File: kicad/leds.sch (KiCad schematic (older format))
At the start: 85 parts, among them U6 74HC154

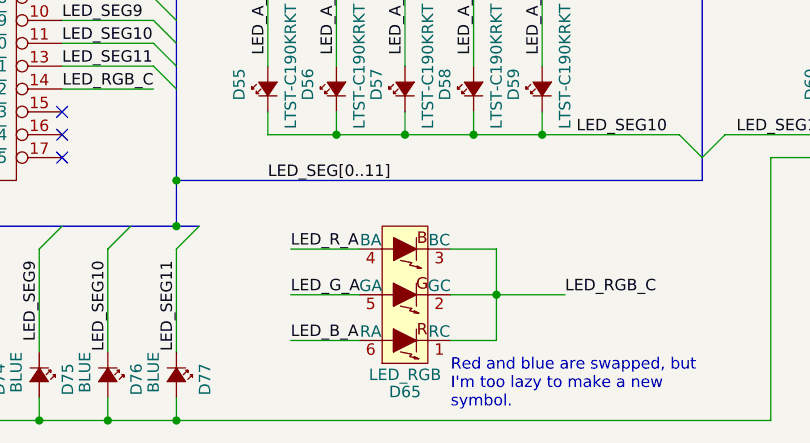
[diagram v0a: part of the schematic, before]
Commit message: Added footprints for most major components
We are missing almost all passives
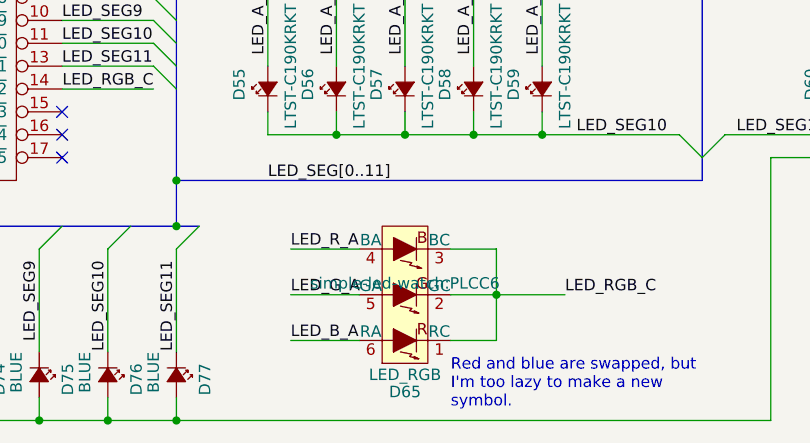
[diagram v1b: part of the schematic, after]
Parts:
- D65: footprint (none) -> simple-led-watch:PLCC6
- U6: footprint (none) -> simple-led-watch:DHVQFN24
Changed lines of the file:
@@
 F 0 "U6" H 3200 4750 50  0000 C CNN
 F 1 "74HC154" H 3200 6550 50  0000 C CNN
-F 2 "" H 3200 5500 50  0001 C CNN
+F 2 "simple-led-watch:DHVQFN24" H 3200 5500 50  0001 C CNN
 F 3 "" H 3200 5500 50  0001 C CNN
 F 4 "568-8858-1-ND" H 3200 5700 60  0001 C CNN "Part No."
@@
 LED_C_MUX3
 $Comp
-L +3.3V #PWR41
+L +3.3V #PWR041
 U 1 1 5802731F
 P 2600 4900
-F 0 "#PWR41" H 2600 4750 50  0001 C CNN
+F 0 "#PWR041" H 2600 4750 50  0001 C CNN
 F 1 "+3.3V" H 2600 5040 50  0000 C CNN
 F 2 "" H 2600 4900 50  0000 C CNN
@@
 $EndComp
 $Comp
-L GND #PWR42
+L GND #PWR042
 U 1 1 5802733F
 P 2600 5200
-F 0 "#PWR42" H 2600 4950 50  0001 C CNN
+F 0 "#PWR042" H 2600 4950 50  0001 C CNN
 F 1 "GND" H 2600 5050 50  0000 C CNN
 F 2 "" H 2600 5200 50  0000 C CNN
@@
 $EndComp
 $Comp
-L +3.3V #PWR40
+L +3.3V #PWR043
 U 1 1 5802739E
 P 2200 4700
-F 0 "#PWR40" H 2200 4550 50  0001 C CNN
+F 0 "#PWR043" H 2200 4550 50  0001 C CNN
 F 1 "+3.3V" H 2200 4840 50  0000 C CNN
 F 2 "" H 2200 4700 50  0000 C CNN
@@
 $EndComp
 $Comp
-L GND #PWR43
+L GND #PWR044
 U 1 1 580273B6
 P 2200 5400
-F 0 "#PWR43" H 2200 5150 50  0001 C CNN
+F 0 "#PWR044" H 2200 5150 50  0001 C CNN
 F 1 "GND" H 2200 5250 50  0000 C CNN
 F 2 "" H 2200 5400 50  0000 C CNN
@@
 $EndComp
 $Comp
-L GND #PWR44
+L GND #PWR045
 U 1 1 5802794D
 P 2600 6600
-F 0 "#PWR44" H 2600 6350 50  0001 C CNN
+F 0 "#PWR045" H 2600 6350 50  0001 C CNN
 F 1 "GND" H 2600 6450 50  0000 C CNN
 F 2 "" H 2600 6600 50  0000 C CNN
@@
 F 0 "D65" H 5200 7525 50  0000 C CNN
 F 1 "LED_RGB" H 5200 7450 50  0000 C CNN
-F 2 "" H 5200 7050 50  0000 C CNN
+F 2 "simple-led-watch:PLCC6" H 5200 7050 50  0000 C CNN
 F 3 "" H 5200 7050 50  0000 C CNN
 F 4 "CLY6D-FKC-CNP1ST1E1BB7D3D3CT-ND" H 5200 7100 60  0001 C CNN "Part No."

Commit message: Completed initial placement of major components
The passives are causing trouble. We need to eliminate every pullup
possible.
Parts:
- C25: footprint (none) -> Capacitors_SMD:C_0402; Part No. (none) -> 1276-1448-1-ND
- C26: footprint (none) -> Capacitors_SMD:C_0402; Part No. (none) -> 1276-1022-1-ND
- R27, R28, R29, R30, R31, R32, R33, R34, R35: footprint (none) -> Resistors_SMD:R_0402
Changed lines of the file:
@@
 LED_C_MUX3
 $Comp
-L +3.3V #PWR041
+L +3.3V #PWR039
 U 1 1 5802731F
 P 2600 4900
-F 0 "#PWR041" H 2600 4750 50  0001 C CNN
+F 0 "#PWR039" H 2600 4750 50  0001 C CNN
 F 1 "+3.3V" H 2600 5040 50  0000 C CNN
 F 2 "" H 2600 4900 50  0000 C CNN
@@
 $EndComp
 $Comp
-L GND #PWR042
+L GND #PWR040
 U 1 1 5802733F
 P 2600 5200
-F 0 "#PWR042" H 2600 4950 50  0001 C CNN
+F 0 "#PWR040" H 2600 4950 50  0001 C CNN
 F 1 "GND" H 2600 5050 50  0000 C CNN
 F 2 "" H 2600 5200 50  0000 C CNN
@@
 F 0 "C26" H 2225 5150 50  0000 L CNN
 F 1 "0.1u" H 2225 4950 50  0000 L CNN
-F 2 "" H 2238 4900 50  0000 C CNN
+F 2 "Capacitors_SMD:C_0402" H 2238 4900 50  0001 C CNN
 F 3 "" H 2200 5050 50  0000 C CNN
+F 4 "1276-1022-1-ND" H 2200 5050 60  0001 C CNN "Part No."
 	1    2200 5050
 	1    0    0    -1
 $EndComp
 $Comp
-L +3.3V #PWR043
+L +3.3V #PWR041
 U 1 1 5802739E
 P 2200 4700
-F 0 "#PWR043" H 2200 4550 50  0001 C CNN
+F 0 "#PWR041" H 2200 4550 50  0001 C CNN
 F 1 "+3.3V" H 2200 4840 50  0000 C CNN
 F 2 "" H 2200 4700 50  0000 C CNN
@@
 $EndComp
 $Comp
-L GND #PWR044
+L GND #PWR042
 U 1 1 580273B6
 P 2200 5400
-F 0 "#PWR044" H 2200 5150 50  0001 C CNN
+F 0 "#PWR042" H 2200 5150 50  0001 C CNN
 F 1 "GND" H 2200 5250 50  0000 C CNN
 F 2 "" H 2200 5400 50  0000 C CNN
@@
 F 0 "C25" H 1725 5150 50  0000 L CNN
 F 1 "1u" H 1725 4950 50  0000 L CNN
-F 2 "" H 1738 4900 50  0000 C CNN
+F 2 "Capacitors_SMD:C_0402" H 1738 4900 50  0001 C CNN
 F 3 "" H 1700 5050 50  0000 C CNN
+F 4 "1276-1448-1-ND" H 1700 5050 60  0001 C CNN "Part No."
 	1    1700 5050
 	1    0    0    -1
 $EndComp
 $Comp
-L GND #PWR045
+L GND #PWR043
 U 1 1 5802794D
 P 2600 6600
-F 0 "#PWR045" H 2600 6350 50  0001 C CNN
+F 0 "#PWR043" H 2600 6350 50  0001 C CNN
 F 1 "GND" H 2600 6450 50  0000 C CNN
 F 2 "" H 2600 6600 50  0000 C CNN
@@
 F 0 "R27" V 1830 800 50  0000 C CNN
 F 1 "R" V 1750 800 50  0000 C CNN
-F 2 "" V 1680 800 50  0000 C CNN
+F 2 "Resistors_SMD:R_0402" V 1680 800 50  0001 C CNN
 F 3 "" H 1750 800 50  0000 C CNN
 	1    1750 800
@@
 F 0 "R28" V 1830 1000 50  0000 C CNN
 F 1 "R" V 1750 1000 50  0000 C CNN
-F 2 "" V 1680 1000 50  0000 C CNN
+F 2 "Resistors_SMD:R_0402" V 1680 1000 50  0001 C CNN
 F 3 "" H 1750 1000 50  0000 C CNN
 	1    1750 1000
@@
 F 0 "R29" V 1830 1200 50  0000 C CNN
 F 1 "R" V 1750 1200 50  0000 C CNN
-F 2 "" V 1680 1200 50  0000 C CNN
+F 2 "Resistors_SMD:R_0402" V 1680 1200 50  0001 C CNN
 F 3 "" H 1750 1200 50  0000 C CNN
 	1    1750 1200
@@
 F 0 "R30" V 1830 1400 50  0000 C CNN
 F 1 "R" V 1750 1400 50  0000 C CNN
-F 2 "" V 1680 1400 50  0000 C CNN
+F 2 "Resistors_SMD:R_0402" V 1680 1400 50  0001 C CNN
 F 3 "" H 1750 1400 50  0000 C CNN
 	1    1750 1400
@@
 F 0 "R31" V 1830 1600 50  0000 C CNN
 F 1 "R" V 1750 1600 50  0000 C CNN
-F 2 "" V 1680 1600 50  0000 C CNN
+F 2 "Resistors_SMD:R_0402" V 1680 1600 50  0001 C CNN
 F 3 "" H 1750 1600 50  0000 C CNN
 	1    1750 1600
@@
 F 0 "R32" V 1830 1800 50  0000 C CNN
 F 1 "R" V 1750 1800 50  0000 C CNN
-F 2 "" V 1680 1800 50  0000 C CNN
+F 2 "Resistors_SMD:R_0402" V 1680 1800 50  0001 C CNN
 F 3 "" H 1750 1800 50  0000 C CNN
 	1    1750 1800
@@
 F 0 "R33" V 1830 3500 50  0000 C CNN
 F 1 "R" V 1750 3500 50  0000 C CNN
-F 2 "" V 1680 3500 50  0000 C CNN
+F 2 "Resistors_SMD:R_0402" V 1680 3500 50  0001 C CNN
 F 3 "" H 1750 3500 50  0000 C CNN
 	1    1750 3500
@@
 F 0 "R34" V 1830 3700 50  0000 C CNN
 F 1 "R" V 1750 3700 50  0000 C CNN
-F 2 "" V 1680 3700 50  0000 C CNN
+F 2 "Resistors_SMD:R_0402" V 1680 3700 50  0001 C CNN
 F 3 "" H 1750 3700 50  0000 C CNN
 	1    1750 3700
@@
 F 0 "R35" V 1830 3900 50  0000 C CNN
 F 1 "R" V 1750 3900 50  0000 C CNN
-F 2 "" V 1680 3900 50  0000 C CNN
+F 2 "Resistors_SMD:R_0402" V 1680 3900 50  0001 C CNN
 F 3 "" H 1750 3900 50  0000 C CNN
 	1    1750 3900

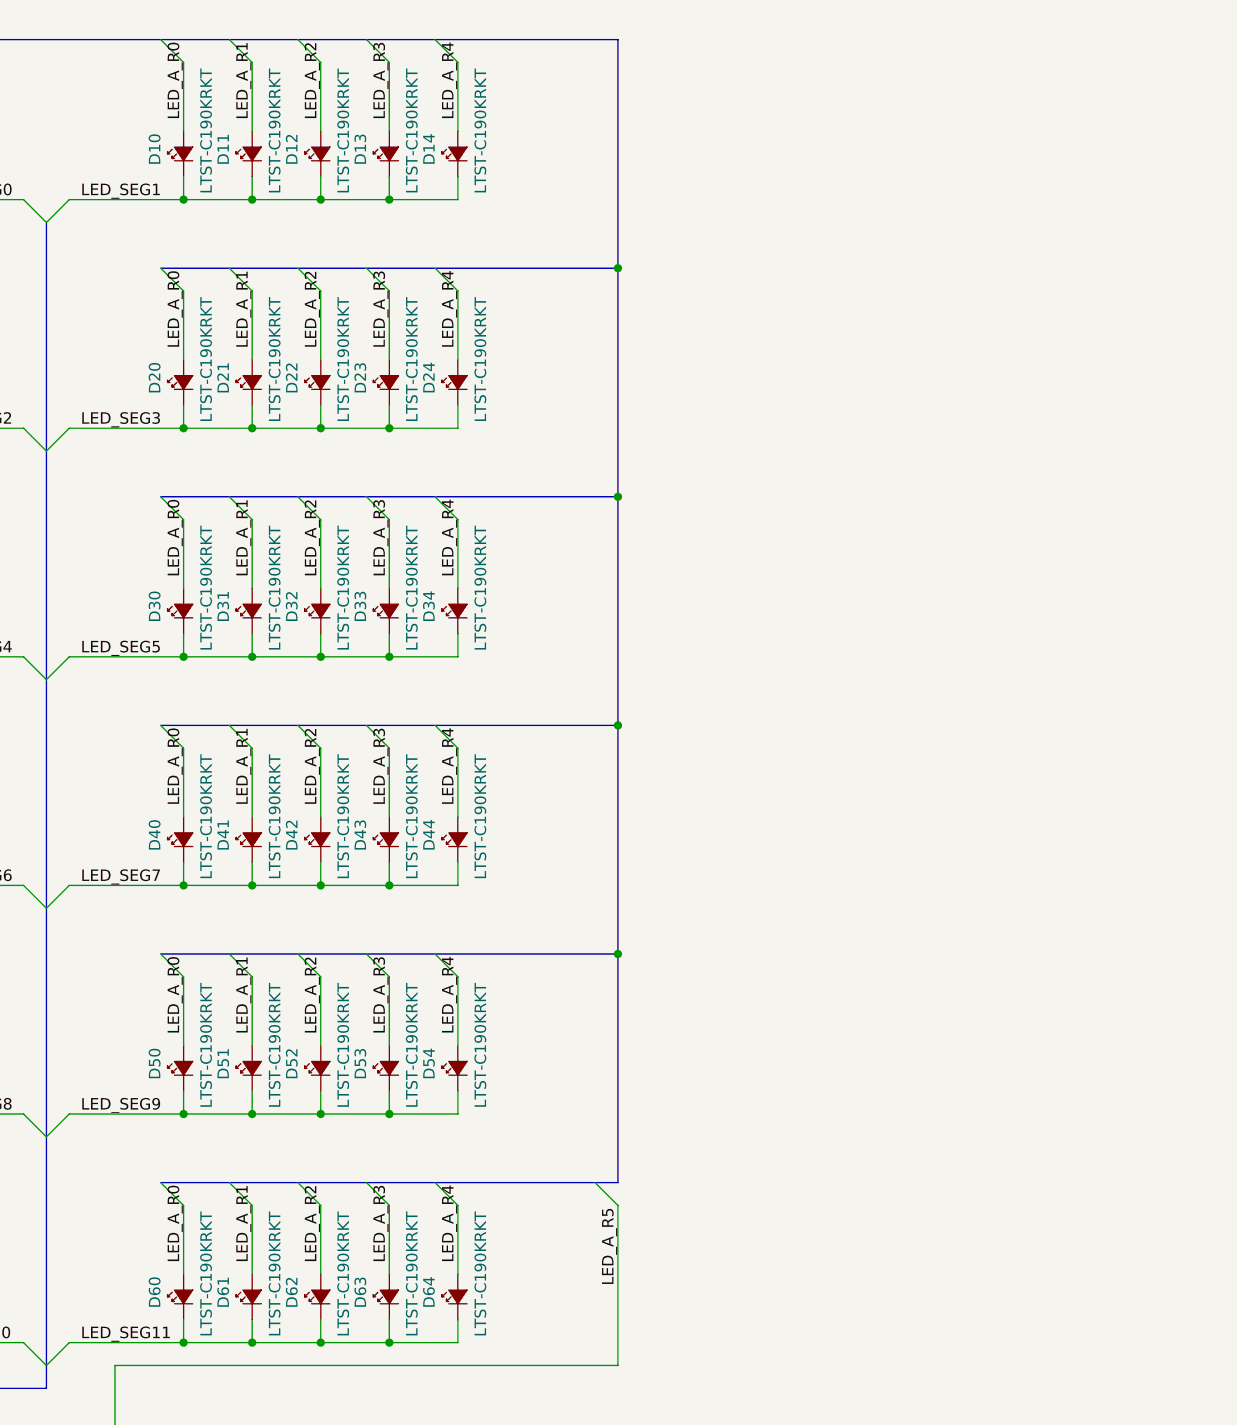
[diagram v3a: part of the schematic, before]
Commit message: Initial route of power and LED ring
I had to do the order swapping thing that I did on the last design
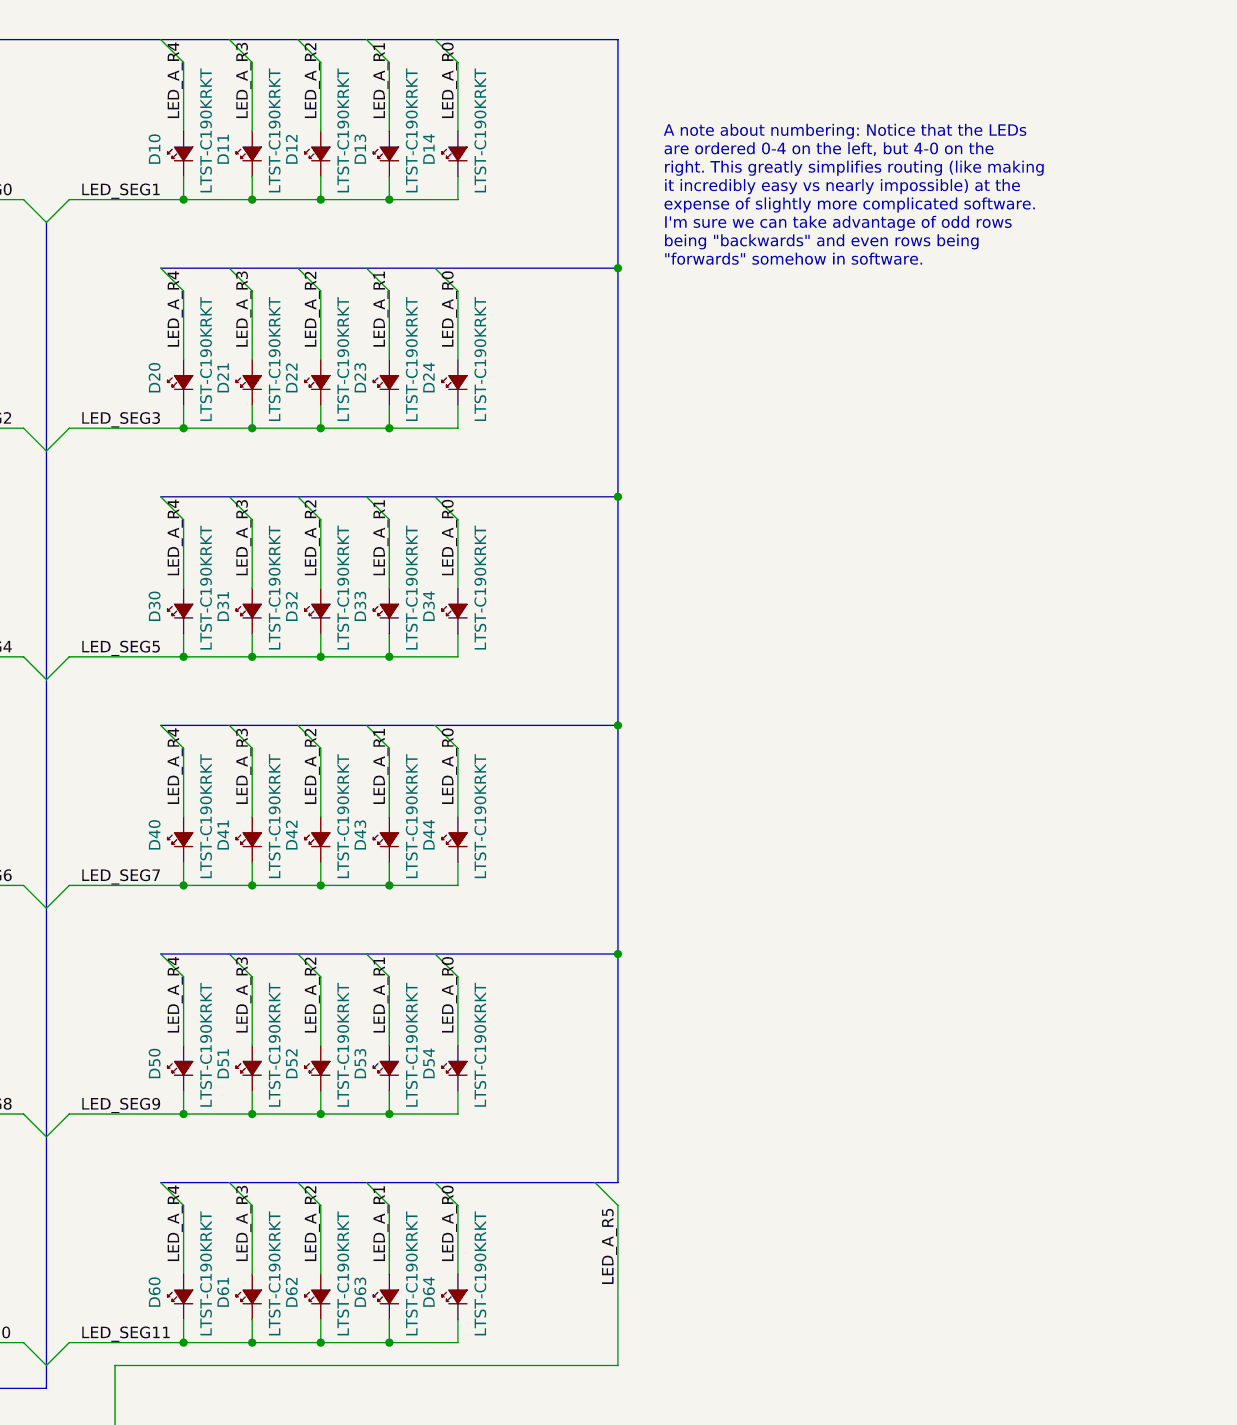
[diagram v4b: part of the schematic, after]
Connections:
- net LED_A_R0: now also D14.2 (A), D24.2 (A), D34.2 (A), D44.2 (A), D54.2 (A), D64.2 (A); no longer D10.2 (A), D20.2 (A), D30.2 (A), D40.2 (A), D50.2 (A), D60.2 (A)
- net LED_A_R1: now also D13.2 (A), D23.2 (A), D33.2 (A), D43.2 (A), D53.2 (A), D63.2 (A); no longer D11.2 (A), D21.2 (A), D31.2 (A), D41.2 (A), D51.2 (A), D61.2 (A)
- net LED_A_R3: now also D11.2 (A), D21.2 (A), D31.2 (A), D41.2 (A), D51.2 (A), D61.2 (A); no longer D13.2 (A), D23.2 (A), D33.2 (A), D43.2 (A), D53.2 (A), D63.2 (A)
- net LED_A_R4: now also D10.2 (A), D20.2 (A), D30.2 (A), D40.2 (A), D50.2 (A), D60.2 (A); no longer D14.2 (A), D24.2 (A), D34.2 (A), D44.2 (A), D54.2 (A), D64.2 (A)
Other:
- note added: "A note about numbering: Notice that the LEDs\nare ordered 0-4 on the left, but 4-0 on the\nright. This greatly simplifies routing (like making\nit incredibly easy vs nearly impossible) at the\nexpense of slightly more complicated software.\nI'm sure we can take advantage of odd rows\nbeing "backwards" and even rows being\n"forwards" somehow in software."
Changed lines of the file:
@@
 	0    -1   -1   0
 $EndComp
-Text Label 7100 3050 1    50   ~ 0
+Text Label 8300 3050 1    50   ~ 0
 LED_A_R0
-Text Label 7400 3050 1    50   ~ 0
+Text Label 8000 3050 1    50   ~ 0
 LED_A_R1
 Text Label 7700 3050 1    50   ~ 0
 LED_A_R2
-Text Label 8000 3050 1    50   ~ 0
+Text Label 7400 3050 1    50   ~ 0
 LED_A_R3
-Text Label 8300 3050 1    50   ~ 0
+Text Label 7100 3050 1    50   ~ 0
 LED_A_R4
 Entry Wire Line
@@
 	0    -1   -1   0
 $EndComp
-Text Label 7100 4050 1    50   ~ 0
+Text Label 8300 4050 1    50   ~ 0
 LED_A_R0
-Text Label 7400 4050 1    50   ~ 0
+Text Label 8000 4050 1    50   ~ 0
 LED_A_R1
 Text Label 7700 4050 1    50   ~ 0
 LED_A_R2
-Text Label 8000 4050 1    50   ~ 0
+Text Label 7400 4050 1    50   ~ 0
 LED_A_R3
-Text Label 8300 4050 1    50   ~ 0
+Text Label 7100 4050 1    50   ~ 0
 LED_A_R4
 Entry Wire Line
@@
 	0    -1   -1   0
 $EndComp
-Text Label 7100 5050 1    50   ~ 0
+Text Label 8300 5050 1    50   ~ 0
 LED_A_R0
-Text Label 7400 5050 1    50   ~ 0
+Text Label 8000 5050 1    50   ~ 0
 LED_A_R1
 Text Label 7700 5050 1    50   ~ 0
 LED_A_R2
-Text Label 8000 5050 1    50   ~ 0
+Text Label 7400 5050 1    50   ~ 0
 LED_A_R3
-Text Label 8300 5050 1    50   ~ 0
+Text Label 7100 5050 1    50   ~ 0
 LED_A_R4
 Entry Wire Line
@@
 	0    -1   -1   0
 $EndComp
-Text Label 7100 6050 1    50   ~ 0
+Text Label 8300 6050 1    50   ~ 0
 LED_A_R0
-Text Label 7400 6050 1    50   ~ 0
+Text Label 8000 6050 1    50   ~ 0
 LED_A_R1
 Text Label 7700 6050 1    50   ~ 0
 LED_A_R2
-Text Label 8000 6050 1    50   ~ 0
+Text Label 7400 6050 1    50   ~ 0
 LED_A_R3
-Text Label 8300 6050 1    50   ~ 0
+Text Label 7100 6050 1    50   ~ 0
 LED_A_R4
 Entry Wire Line
@@
 Entry Wire Line
 	7000 1700 7100 1800
-Text Label 8300 2050 1    50   ~ 0
+Text Label 7100 2050 1    50   ~ 0
 LED_A_R4
-Text Label 8000 2050 1    50   ~ 0
+Text Label 7400 2050 1    50   ~ 0
 LED_A_R3
 Text Label 7700 2050 1    50   ~ 0
 LED_A_R2
-Text Label 7400 2050 1    50   ~ 0
+Text Label 8000 2050 1    50   ~ 0
 LED_A_R1
-Text Label 7100 2050 1    50   ~ 0
+Text Label 8300 2050 1    50   ~ 0
 LED_A_R0
 $Comp
@@
 Entry Wire Line
 	7000 700  7100 800
-Text Label 8300 1050 1    50   ~ 0
+Text Label 7100 1050 1    50   ~ 0
 LED_A_R4
-Text Label 8000 1050 1    50   ~ 0
+Text Label 7400 1050 1    50   ~ 0
 LED_A_R3
 Text Label 7700 1050 1    50   ~ 0
 LED_A_R2
-Text Label 7400 1050 1    50   ~ 0
+Text Label 8000 1050 1    50   ~ 0
 LED_A_R1
-Text Label 7100 1050 1    50   ~ 0
+Text Label 8300 1050 1    50   ~ 0
 LED_A_R0
 $Comp
@@
 NoConn ~ 3700 6400
 NoConn ~ 3700 6500
+Text Notes 9200 1700 0    50   ~ 0
+A note about numbering: Notice that the LEDs\nare ordered 0-4 on the left, but 4-0 on the\nright. This greatly simplifies routing (like making\nit incredibly easy vs nearly impossible) at the\nexpense of slightly more complicated software.\nI'm sure we can take advantage of odd rows\nbeing "backwards" and even rows being\n"forwards" somehow in software.
 $EndSCHEMATC

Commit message: Selected programming header
Only one non-connected trace left. And I don't know where it is...
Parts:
- removed C25: 1u, Capacitors_SMD:C_0402, symbol C
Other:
- note added: "C25: 1uF\n\nNo way it could fit..."
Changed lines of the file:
@@
 LED_C_MUX3
 $Comp
-L +3.3V #PWR037
+L +3.3V #PWR036
 U 1 1 5802731F
 P 2600 4900
-F 0 "#PWR037" H 2600 4750 50  0001 C CNN
+F 0 "#PWR036" H 2600 4750 50  0001 C CNN
 F 1 "+3.3V" H 2600 5040 50  0000 C CNN
 F 2 "" H 2600 4900 50  0000 C CNN
@@
 $EndComp
 $Comp
-L GND #PWR038
+L GND #PWR037
 U 1 1 5802733F
 P 2600 5200
-F 0 "#PWR038" H 2600 4950 50  0001 C CNN
+F 0 "#PWR037" H 2600 4950 50  0001 C CNN
 F 1 "GND" H 2600 5050 50  0000 C CNN
 F 2 "" H 2600 5200 50  0000 C CNN
@@
 $EndComp
 $Comp
-L +3.3V #PWR039
+L +3.3V #PWR038
 U 1 1 5802739E
 P 2200 4700
-F 0 "#PWR039" H 2200 4550 50  0001 C CNN
+F 0 "#PWR038" H 2200 4550 50  0001 C CNN
 F 1 "+3.3V" H 2200 4840 50  0000 C CNN
 F 2 "" H 2200 4700 50  0000 C CNN
@@
 $EndComp
 $Comp
-L GND #PWR040
+L GND #PWR039
 U 1 1 580273B6
 P 2200 5400
-F 0 "#PWR040" H 2200 5150 50  0001 C CNN
+F 0 "#PWR039" H 2200 5150 50  0001 C CNN
 F 1 "GND" H 2200 5250 50  0000 C CNN
 F 2 "" H 2200 5400 50  0000 C CNN
@@
 $EndComp
 $Comp
-L C C25
-U 1 1 580276EE
-P 1700 5050
-F 0 "C25" H 1725 5150 50  0000 L CNN
-F 1 "1u" H 1725 4950 50  0000 L CNN
-F 2 "Capacitors_SMD:C_0402" H 1738 4900 50  0001 C CNN
-F 3 "" H 1700 5050 50  0000 C CNN
-F 4 "1276-1448-1-ND" H 1700 5050 60  0001 C CNN "Part No."
-	1    1700 5050
-	1    0    0    -1
-$EndComp
-$Comp
-L GND #PWR041
+L GND #PWR040
 U 1 1 5802794D
 P 2600 6600
-F 0 "#PWR041" H 2600 6350 50  0001 C CNN
+F 0 "#PWR040" H 2600 6350 50  0001 C CNN
 F 1 "GND" H 2600 6450 50  0000 C CNN
 F 2 "" H 2600 6600 50  0000 C CNN
@@
 Text Notes 9200 1700 0    50   ~ 0
 A note about numbering: Notice that the LEDs\nare ordered 0-4 on the left, but 4-0 on the\nright. This greatly simplifies routing (like making\nit incredibly easy vs nearly impossible) at the\nexpense of slightly more complicated software.\nI'm sure we can take advantage of odd rows\nbeing "backwards" and even rows being\n"forwards" somehow in software.
+Text Notes 1250 5150 0    50   ~ 0
+C25: 1uF\n\nNo way it could fit...
 $EndSCHEMATC

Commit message: Placed parts for round two
I'm pretty sure I can do it better
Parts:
- added C25: 1u, Capacitors_SMD:C_0402, symbol C
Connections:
- net +3V3: now also C25.1
- net GND: now also C25.2
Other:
- note removed: "C25: 1uF\n\nNo way it could fit..."
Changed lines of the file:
@@
 Text Notes 9200 1700 0    50   ~ 0
 A note about numbering: Notice that the LEDs\nare ordered 0-4 on the left, but 4-0 on the\nright. This greatly simplifies routing (like making\nit incredibly easy vs nearly impossible) at the\nexpense of slightly more complicated software.\nI'm sure we can take advantage of odd rows\nbeing "backwards" and even rows being\n"forwards" somehow in software.
-Text Notes 1250 5150 0    50   ~ 0
-C25: 1uF\n\nNo way it could fit...
+$Comp
+L C C25
+U 1 1 58084349
+P 1700 5050
+F 0 "C25" H 1725 5150 50  0000 L CNN
+F 1 "1u" H 1725 4950 50  0000 L CNN
+F 2 "Capacitors_SMD:C_0402" H 1738 4900 50  0001 C CNN
+F 3 "" H 1700 5050 50  0000 C CNN
+F 4 "1276-1448-1-ND" H 1700 5050 60  0001 C CNN "Part No."
+	1    1700 5050
+	1    0    0    -1
+$EndComp
 $EndSCHEMATC
